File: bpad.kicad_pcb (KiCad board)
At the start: 2 copper layers, 76.2 x 94.5 mm, 53 parts, among them J1 USB_B_Mini, SW0 0, SW1 1, SW2 2, SW3 3, SW4 4, SW5 5, SW6 6, SW7 7, SW8 8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

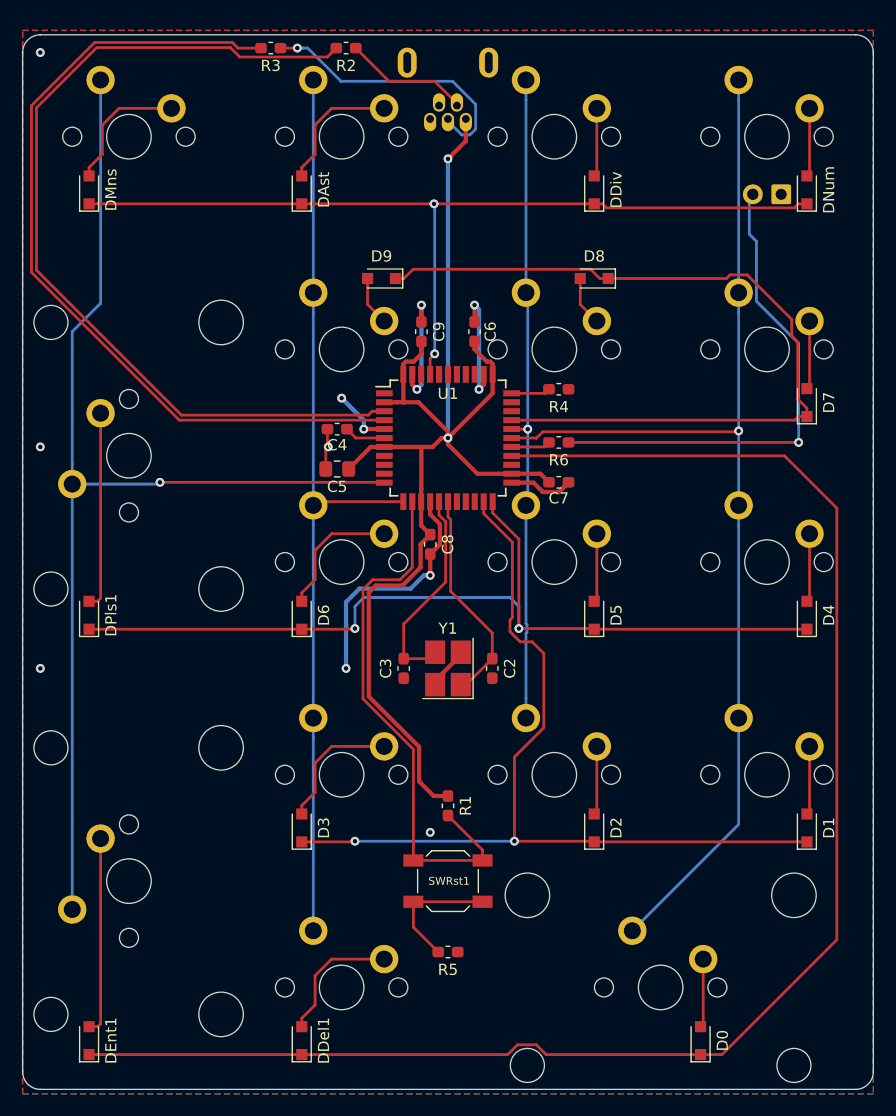
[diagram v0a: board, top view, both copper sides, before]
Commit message: moved the usb around and added label
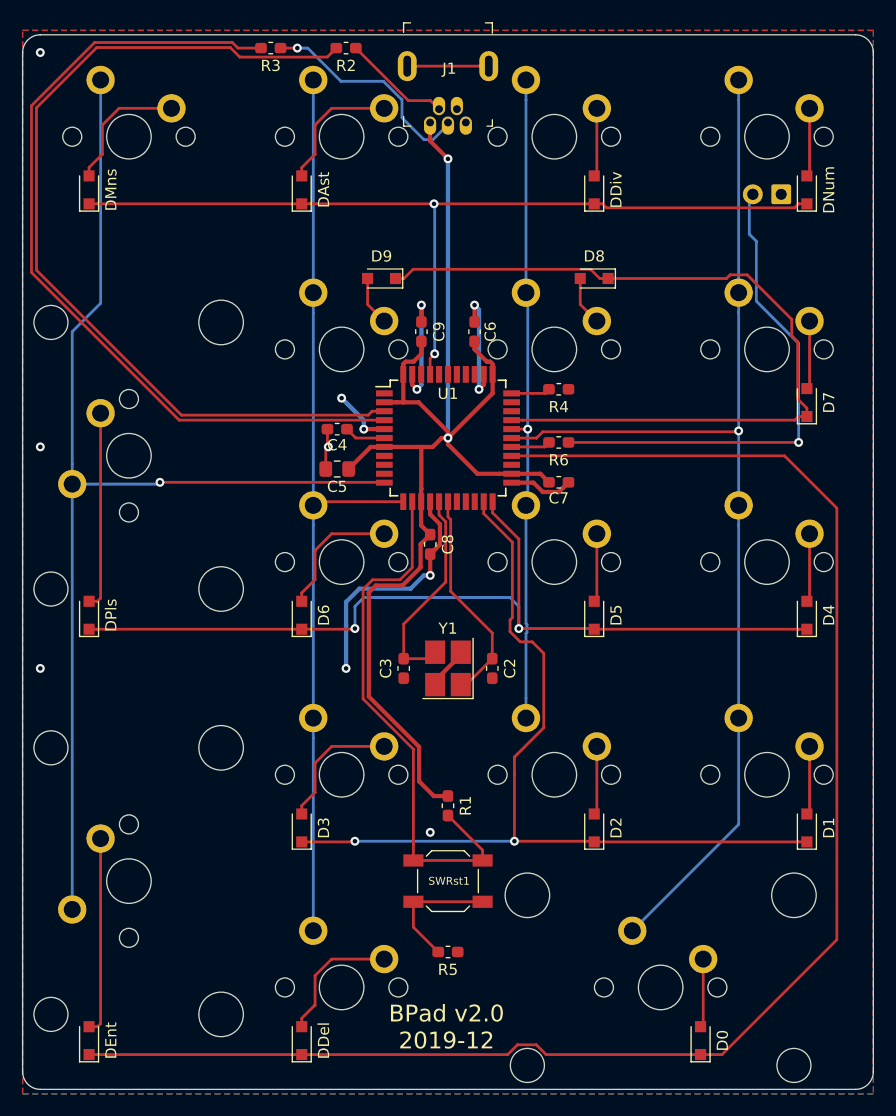
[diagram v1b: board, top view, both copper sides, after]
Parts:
- J1: footprint digikey-kicad-library:USB_Mini_B_Female_548190519 -> LocalFootprints:USB_Mini_B_Female_548190519_top; moved to F.Cu
- moved J1 0.32 mm to (28.6, -1.27)
- renumbered DDel1 to DDel, DEnt1 to DEnt, DPls1 to DPls
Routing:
- net Net-(J1-PadSH): track 0.00 -> 7.30 mm
- net Net-(J1-Pad3): track 25.2 -> 20.3 mm
- net Net-(J1-Pad2): track 11.3 -> 9.72 mm
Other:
- board text added: "BPad v2.0 2019-12"

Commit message: ordered v2
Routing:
- net Net-(J1-Pad2): track 9.72 -> 11.6 mm
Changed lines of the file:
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@@
     (thickness 1.6)
     (drawings 13)
-    (tracks 378)
+    (tracks 380)
     (zones 0)
     (modules 53)
@@
       (effects (font (size 1 1) (thickness 0.15)))
     )
-    (fp_text value USB_B_Mini (at -4.2 6.35 270) (layer F.Fab)
+    (fp_text value USB_B_Mini (at -4.2 6.35 90) (layer F.Fab)
       (effects (font (size 1 1) (thickness 0.15)))
     )
@@
     (fp_line (start -9.05 -4.75) (end -9.05 4.75) (layer F.CrtYd) (width 0.05))
     (fp_line (start 1.35 -4.75) (end 1.35 4.75) (layer F.CrtYd) (width 0.05))
-    (fp_text user %R (at -5.7 -0.075 270) (layer F.Fab)
+    (fp_text user %R (at -5.7 -0.075 90) (layer F.Fab)
       (effects (font (size 1 1) (thickness 0.15)))
     )
@@
     (pad SH thru_hole oval (at -5.05 -3.65 270) (size 2.7 1.7) (drill oval 1.9 0.7) (layers *.Cu *.Mask)
       (net 27 "Net-(J1-PadSH)"))
-    (pad 2 thru_hole oval (at -1.2 0.8 270) (size 1.65 1.1) (drill 0.7 (offset -0.275 0)) (layers *.Cu *.Mask)
+    (pad 4 thru_hole oval (at -1.2 0.8 270) (size 1.65 1.1) (drill 0.7 (offset -0.275 0)) (layers *.Cu *.Mask)
+      (net 29 "Net-(J1-Pad4)"))
+    (pad 2 thru_hole oval (at -1.2 -0.8 270) (size 1.65 1.1) (drill 0.7 (offset -0.275 0)) (layers *.Cu *.Mask)
       (net 28 "Net-(J1-Pad2)"))
-    (pad 4 thru_hole oval (at -1.2 -0.8 270) (size 1.65 1.1) (drill 0.7 (offset -0.275 0)) (layers *.Cu *.Mask)
-      (net 29 "Net-(J1-Pad4)"))
-    (pad 1 thru_hole oval (at 0 1.6 270) (size 1.65 1.1) (drill 0.7 (offset 0.275 0)) (layers *.Cu *.Mask)
+    (pad 5 thru_hole oval (at 0 1.6 270) (size 1.65 1.1) (drill 0.7 (offset 0.275 0)) (layers *.Cu *.Mask)
+      (net 1 GND))
+    (pad 1 thru_hole oval (at 0 -1.6 270) (size 1.65 1.1) (drill 0.7 (offset 0.275 0)) (layers *.Cu *.Mask)
       (net 30 +5V))
-    (pad 5 thru_hole oval (at 0 -1.6 270) (size 1.65 1.1) (drill 0.7 (offset 0.275 0)) (layers *.Cu *.Mask)
-      (net 1 GND))
     (pad 3 thru_hole oval (at 0 0 270) (size 1.65 1.1) (drill 0.7 (offset 0.275 0)) (layers *.Cu *.Mask)
       (net 31 "Net-(J1-Pad3)"))
@@
   (segment (start -2.54 24.765) (end -2.54 41.330625) (width 0.25) (layer F.Cu) (net 26))
   (segment (start 24.925 -6.32) (end 32.225 -6.32) (width 0.25) (layer F.Cu) (net 27))
-  (segment (start 27.013 -3.232) (end 27.775 -2.47) (width 0.25) (layer F.Cu) (net 28))
-  (segment (start 20.321875 -7.9375) (end 25.027375 -3.232) (width 0.25) (layer F.Cu) (net 28))
-  (segment (start 25.027375 -3.232) (end 27.013 -3.232) (width 0.25) (layer F.Cu) (net 28))
-  (segment (start 29.375 -2.7875) (end 29.375 -2.974951) (width 0.25) (layer F.Cu) (net 29))
+  (segment (start 29.375 -2.7875) (end 29.375 -2.974951) (width 0.25) (layer F.Cu) (net 28))
+  (segment (start 20.820947 -7.438428) (end 20.321875 -7.9375) (width 0.25) (layer F.Cu) (net 28))
+  (segment (start 23.614385 -4.64499) (end 20.820947 -7.438428) (width 0.25) (layer F.Cu) (net 28))
+  (segment (start 27.387461 -4.64499) (end 23.614385 -4.64499) (width 0.25) (layer F.Cu) (net 28))
+  (segment (start 29.375 -2.657451) (end 27.387461 -4.64499) (width 0.25) (layer F.Cu) (net 28))
+  (segment (start 29.375 -2.47) (end 29.375 -2.657451) (width 0.25) (layer F.Cu) (net 28))
   (via (at 28.575 1.984375) (size 0.8) (drill 0.4) (layers F.Cu B.Cu) (net 30))
   (via (at 28.575 26.9875) (size 0.8) (drill 0.4) (layers F.Cu B.Cu) (net 30))
@@
   (segment (start 22.106365 40.20301) (end 21.481136 40.828239) (width 0.381) (layer F.Cu) (net 30))
   (segment (start 21.481136 40.828239) (end 21.481136 50.141494) (width 0.381) (layer F.Cu) (net 30))
-  (segment (start 26.975 0.384375) (end 28.575 1.984375) (width 0.381) (layer F.Cu) (net 30))
-  (segment (start 26.975 -1.27) (end 26.975 0.384375) (width 0.381) (layer F.Cu) (net 30))
+  (segment (start 30.175 0.384375) (end 28.575 1.984375) (width 0.381) (layer F.Cu) (net 30))
+  (segment (start 30.175 -1.27) (end 30.175 0.384375) (width 0.381) (layer F.Cu) (net 30))
   (via (at 15.08125 -7.9375) (size 0.8) (drill 0.4) (layers F.Cu B.Cu) (net 31))
   (segment (start 13.575 -7.9375) (end 15.08125 -7.9375) (width 0.25) (layer F.Cu) (net 31))
